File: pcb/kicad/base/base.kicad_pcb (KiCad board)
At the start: 2 copper layers, 381 parts, among them P1 J-Link SWD, P10 CONN_01X02, P11 CONN_01X02, P2 SMA, P3 CONN_01X02, P4 USB Micro B, P5 Button, P6 Button, P7 Button, P8 Button, P9 Button, Q1 IRLML2502, U1 SAMB11G18A-edit, U2 XBee-PRO_900HP, Y1 32.768kHz, Y2 26MHz

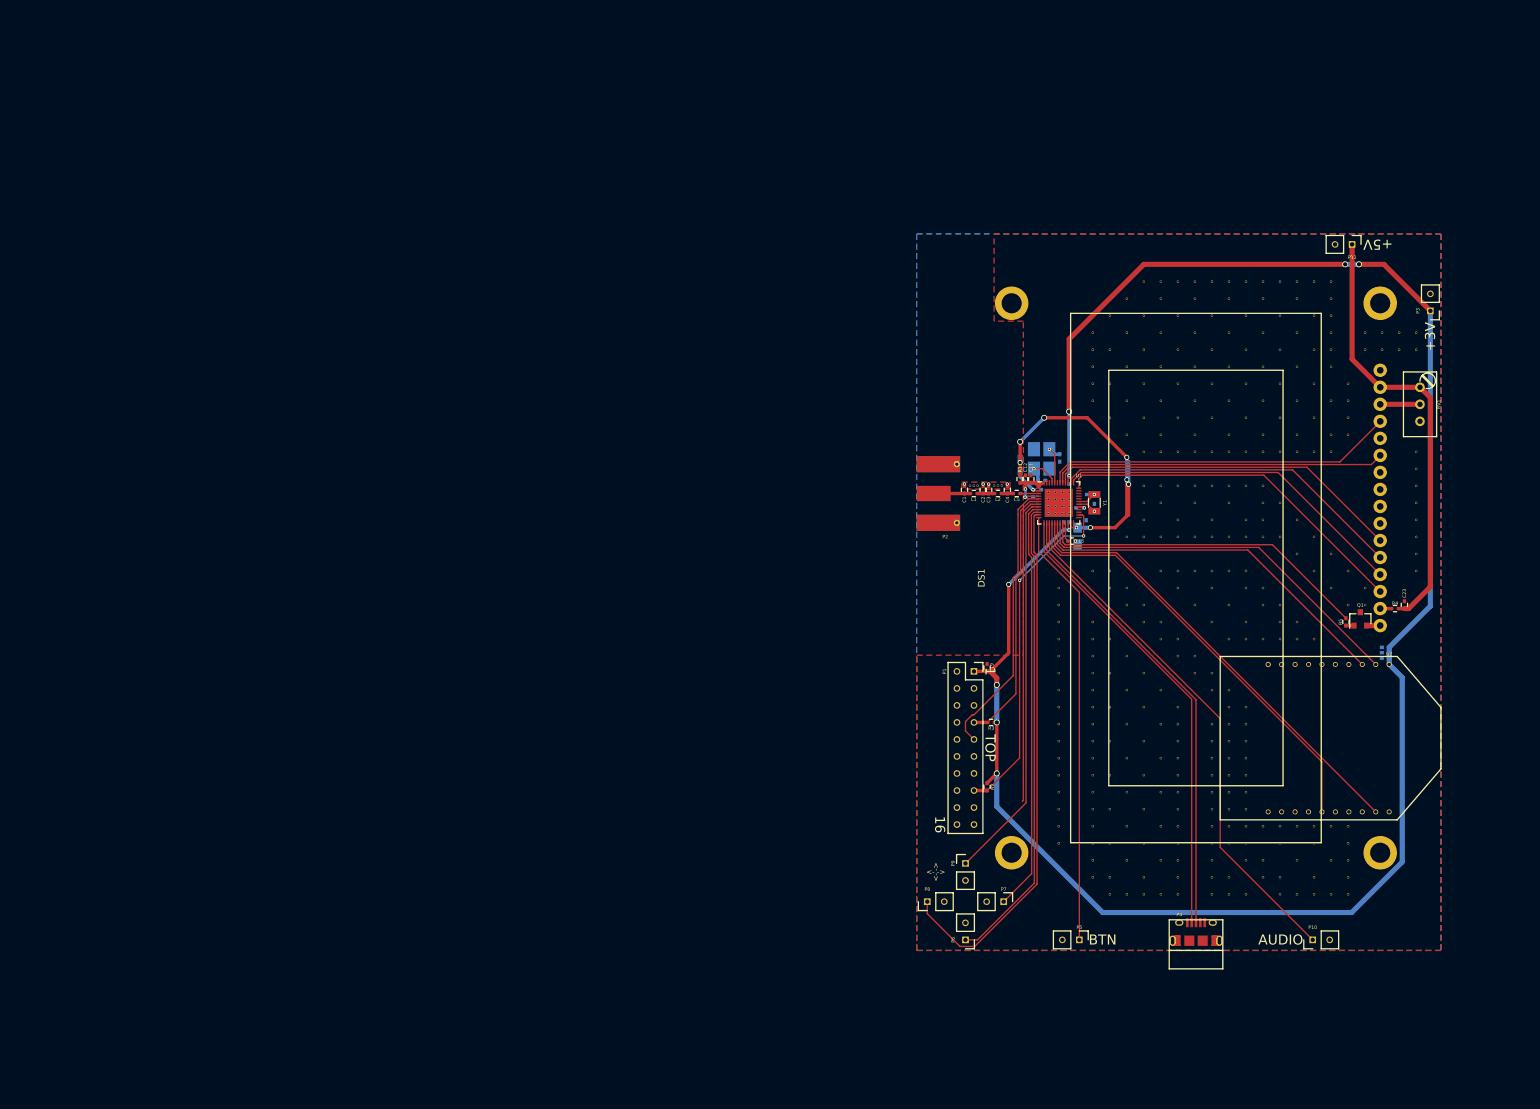
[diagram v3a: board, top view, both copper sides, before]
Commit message: Revamp base station layout
26MHz crystal moved to the top layer after reducing pad size. Slight
spacing with SMD components to avoid difficulties with hand soldering.
Component sections moved around for a more compact final layout. Antenna
section still needs to changed depending on transmission line matching
circuit. Traces to be finished.
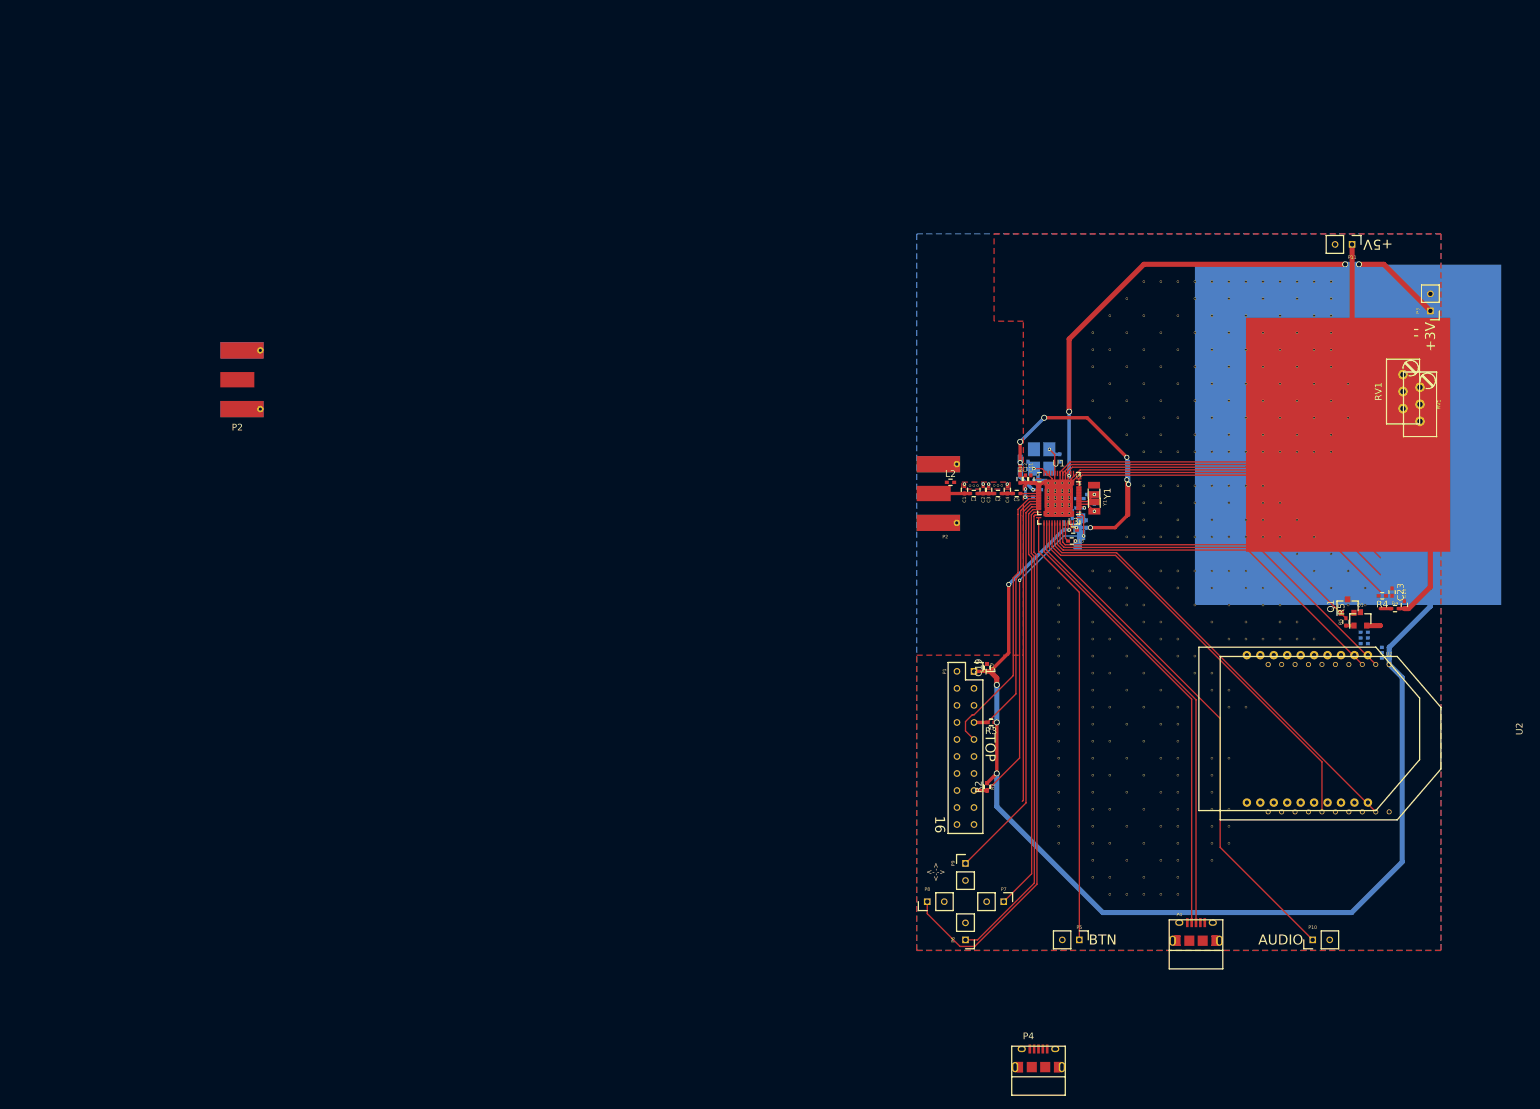
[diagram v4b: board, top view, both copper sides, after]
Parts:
- removed the C19 at (119.3, 95.3)
- removed DS1: LCD16X4, CFAH1604A
- removed the R2 at (119.3, 113.1)
- removed the R3 at (119.9, 103.5)
- removed the REF** at (178.3, 47.9)
- removed the REF** at (180.8, 47.9)
- removed the REF** at (183.4, 47.9)
- removed the REF** at (183.4, 65.7)
- removed the REF** at (183.4, 63.1)
- removed the REF** at (183.4, 73.3)
- removed the REF** at (183.4, 75.8)
- removed the REF** at (183.4, 70.7)
- removed the REF** at (183.4, 68.2)
- removed the REF** at (183.4, 78.4)
- removed the REF** at (173.2, 55.5)
- removed the REF** at (183.4, 80.9)
- removed the REF** at (173.2, 129.2)
- removed the REF** at (165.6, 129.2)
- removed the REF** at (163.0, 129.2)
- removed the REF** at (168.1, 129.2)
- removed the REF** at (170.7, 129.2)
- removed the REF** at (160.5, 124.1)
- removed the REF** at (160.5, 126.6)
- removed the REF** at (168.1, 126.6)
- removed the REF** at (163.0, 126.6)
- removed the REF** at (145.3, 40.3)
- removed the REF** at (165.6, 124.1)
- removed the REF** at (170.7, 124.1)
- removed the REF** at (173.2, 124.1)
- removed the REF** at (173.2, 126.6)
- removed the REF** at (173.2, 121.5)
- removed the REF** at (173.2, 119.0)
- removed the REF** at (165.6, 119.0)
- removed the REF** at (163.0, 119.0)
- removed the REF** at (168.1, 119.0)
- removed the REF** at (170.7, 119.0)
- removed the REF** at (135.1, 53.0)
- removed the REF** at (163.0, 121.5)
- removed the REF** at (168.1, 121.5)
- removed the REF** at (160.5, 119.0)
- removed the REF** at (158.0, 121.5)
- removed the REF** at (158.0, 119.0)
- removed the REF** at (158.0, 116.5)
- removed the REF** at (158.0, 124.1)
- removed the REF** at (158.0, 113.9)
- removed the REF** at (158.0, 111.4)
- removed the REF** at (158.0, 108.8)
- removed the REF** at (158.0, 103.8)
- removed the REF** at (158.0, 106.3)
- removed the REF** at (155.4, 129.2)
- removed the REF** at (152.9, 129.2)
- removed the REF** at (155.4, 126.6)
- removed the REF** at (152.9, 126.6)
- removed the REF** at (158.0, 129.2)
- removed the REF** at (152.9, 106.3)
- removed the REF** at (152.9, 103.8)
- removed the REF** at (155.4, 103.8)
- removed the REF** at (180.8, 45.3)
- removed the REF** at (155.4, 106.3)
- removed the REF** at (155.4, 113.9)
- removed the REF** at (155.4, 111.4)
- removed the REF** at (178.3, 45.3)
- removed the REF** at (175.7, 45.3)
- removed the REF** at (175.7, 47.9)
- added C12: 0.1uF, Capacitors_SMD:C_0402, B.Cu at (126.9, 66.5)
- added C13: 0.1uF, Capacitors_SMD:C_0402, B.Cu at (126.9, 67.4)
- added C14: 4.7uF 6.3V, Capacitors_SMD:C_0402, B.Cu at (132.0, 72.5)
- added C15: 0.1uF, Capacitors_SMD:C_0402, B.Cu at (131.6, 66.2)
- added C16: 2.2uF 6.3V, Capacitors_SMD:C_0402, B.Cu at (131.4, 73.9)
- added C18: 1.0uF, Capacitors_SMD:C_0402, B.Cu at (133.2, 70.1)
- added C19 (x2): C_Small, Capacitors_SMD:C_0402, F.Cu at (119.3, 95.3)
- added C20: 47pF, Capacitors_SMD:C_0402, B.Cu at (175.6, 91.7)
- added C21: 1.0uF, Capacitors_SMD:C_0402, B.Cu at (175.6, 90.9)
- added C22: 10uF, Capacitors_SMD:C_0402, B.Cu at (175.6, 90.0)
- added C23: 1.0uF, Capacitors_SMD:C_0402, F.Cu at (179.8, 84.1)
- added FB1: BLM03AG121SN1, Capacitors_SMD:C_0603_HandSoldering, B.Cu at (124.3, 65.5)
- added L2: 3nH, Capacitors_SMD:C_0402, F.Cu at (113.9, 67.7)
- added L3: 9.1nH, Capacitors_SMD:C_0402, F.Cu at (132.2, 74.8)
- added L4: 4.7uH, Capacitors_SMD:C_0805_HandSoldering, B.Cu at (133.4, 74.3)
- added P2: SMA, Misc:Molex_SMA_Jack_Edge_Mount, F.Cu at (9.16, 52.4)
- added P4: USB Micro B, Connectors:USB_Micro-B_10118194-000XLF, F.Cu at (127.0, 154.9)
- added Q1: IRLML2502, TO_SOT_Packages_SMD:SOT-23, F.Cu at (173.1, 86.1)
- added R1: 0, Capacitors_SMD:C_0402, B.Cu at (125.4, 65.1)
- added R2 (x2): 10k, Capacitors_SMD:C_0402, F.Cu at (119.3, 113.1)
- added R3 (x2): 100k, Capacitors_SMD:C_0402, F.Cu at (119.9, 103.5)
- added R4: 100, Capacitors_SMD:C_0402, F.Cu at (178.3, 84.6)
- added R5: 1k, Capacitors_SMD:C_0402, F.Cu at (170.9, 86.6)
- added RV1: 10k, Potentiometers:Potentiometer_Trimmer_Bourns_3296W, F.Cu at (181.4, 51.6)
- added U1: SAMB11G18A-edit, Housings:QFN-48-1EP_6x6mm_Pitch0.4mm, F.Cu at (130.0, 69.3)
- added U2: XBee-PRO_900HP, Digi_XBee-PRO_TH, F.Cu at (173.8, 104.5)
- added Y1: 32.768kHz, Crystals:Crystal_SMD_3215-2pin_3.2x1.5mm, F.Cu at (135.3, 69.3)
- REF**: value Via_Stitch_Dia0.356mm_Drill0.254mm -> Antenna_Shield
- REF**: value Via_Stitch_Dia0.356mm_Drill0.254mm -> (none)
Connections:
- REF** pad 1: GND -> (no net)
- REF** pad 1: GND -> /DISP_BRIGHT
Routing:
- net 78: track 0.00 -> 79.9 mm
- net /BTN_DOWN: track 79.9 -> 0.00 mm
- net 70: track 0.00 -> 78.5 mm
- net /AUDIO_SIG: track 78.5 -> 0.00 mm
- net 76: track 0.00 -> 70.2 mm
- net /BTN_RIGHT: track 70.2 -> 0.00 mm
- net 67: track 0.00 -> 68.9 mm
- net /Data+: track 68.9 -> 0.00 mm
- net 66: track 0.00 -> 68.8 mm
- net /Data-: track 68.8 -> 0.00 mm
- net 45: track 0.00 -> 67.7 mm
- net /UART_CTS: track 67.7 -> 0.00 mm
- net /+5V: track 65.5 -> 0.00 mm
- net 75: track 0.00 -> 65.5 mm
- net /BTN_HELP: track 65.5 -> 0.00 mm
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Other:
- net class Power removed

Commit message: Update base component placement and routing
New base station revision updated for a more complete prototype. Buttons
placed into layout, and SWD debugger pin header fixed.
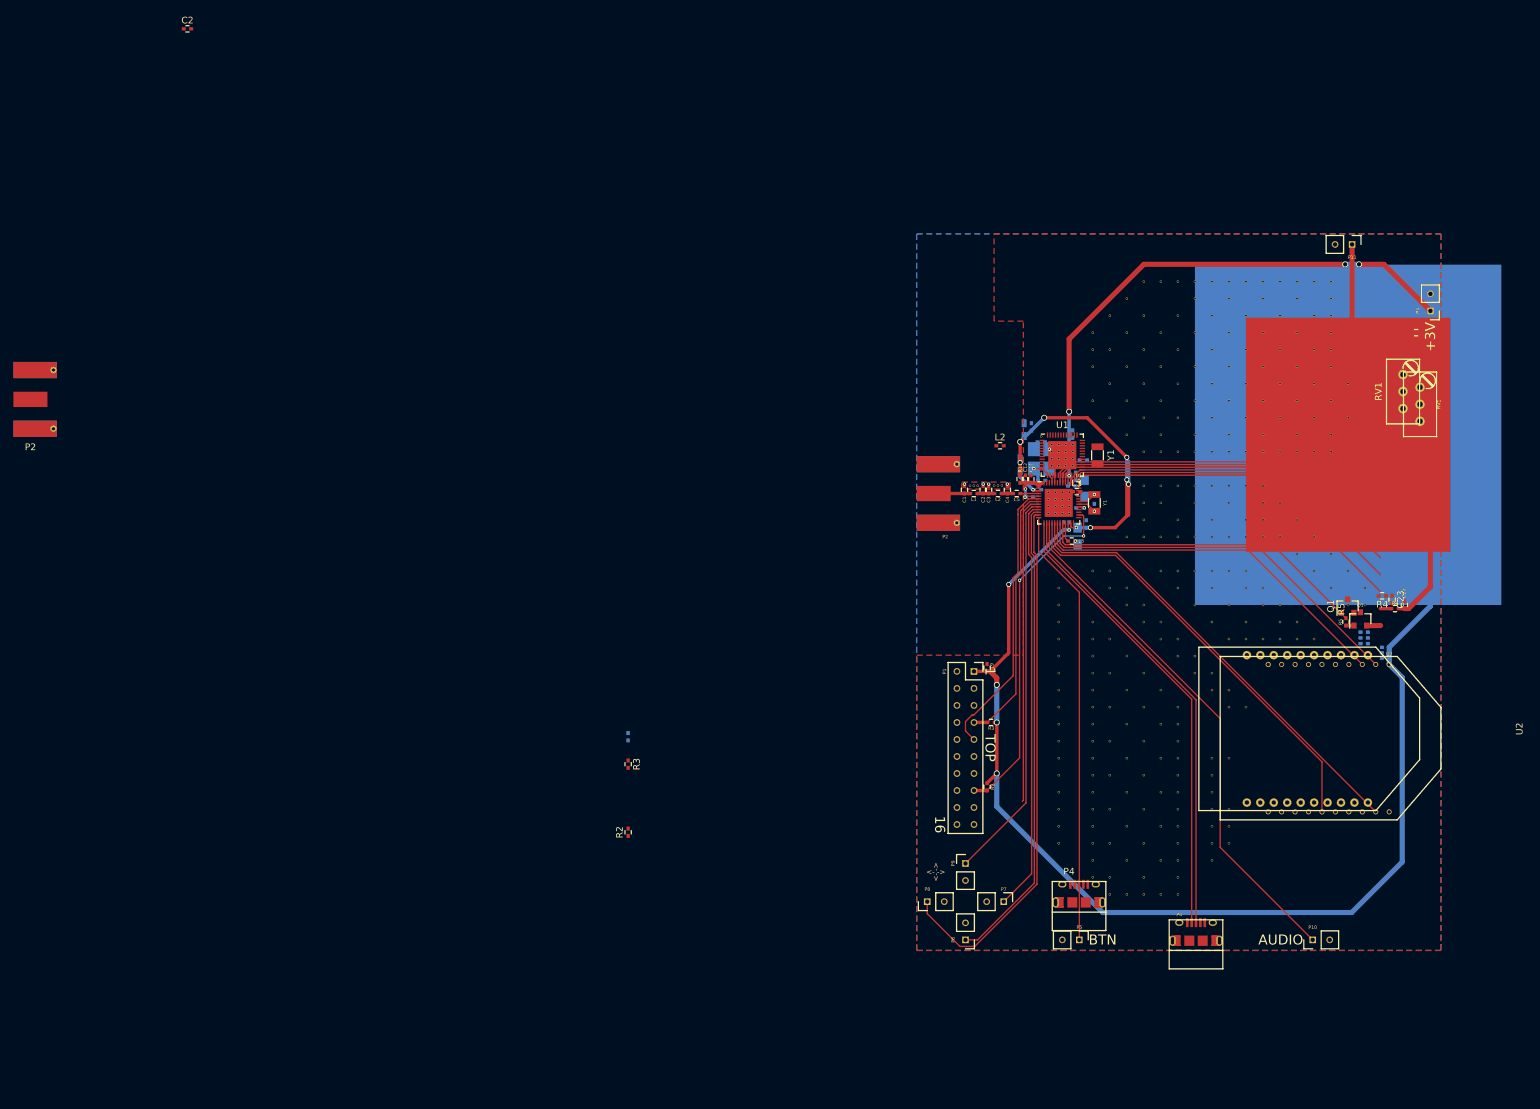
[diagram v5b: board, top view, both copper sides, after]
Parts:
- removed the C19 at (119.3, 95.3) (x2)
- removed the R2 at (119.3, 113.1) (x2)
- removed the R3 at (119.9, 103.5) (x2)
- added C19: C_Small, Capacitors_SMD:C_0402, B.Cu at (65.8, 105.6)
- added C19: C_Small, Capacitors_SMD:C_0402, F.Cu at (119.3, 95.3)
- added C2: DNI, Capacitors_SMD:C_0402, F.Cu at (0.00, 0.00)
- added R2: 10k, Capacitors_SMD:C_0402, F.Cu at (65.8, 119.9)
- added R2: 10k, Capacitors_SMD:C_0402, F.Cu at (119.3, 113.1)
- added R3: 100k, Capacitors_SMD:C_0402, F.Cu at (65.8, 109.7)
- added R3: 100k, Capacitors_SMD:C_0402, F.Cu at (119.9, 103.5)
- moved P2 31.0 mm to (-21.7, 55.3)
- moved P4 25.3 mm to (133.1, 130.4)
- moved L2 9.19 mm to (121.3, 62.2)
- moved C15 5.75 mm to (132.1, 60.5)
- moved C13 5.75 mm to (127.4, 61.7)
- moved FB1 5.75 mm to (124.8, 59.8)
- moved R1 5.75 mm to (125.9, 59.4)
- moved U1 5.75 mm to (130.6, 63.6)
- moved Y1 5.75 mm to (135.8, 63.6)
- moved C16 5.75 mm to (132.0, 68.2)
- moved L3 5.75 mm to (132.7, 69.1)
- moved L4 5.75 mm to (133.9, 68.6)
- moved C12 5.75 mm to (127.4, 60.8)
- moved C14 5.75 mm to (132.6, 66.8)
- moved C18 5.75 mm to (133.7, 64.4)
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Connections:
- U1 pad 10: /BTN_RIGHT -> /BTN_UP
- U1 pad 11: /BTN_DOWN -> /BTN_RIGHT
- U1 pad 9: /BTN_UP -> /BTN_DOWN
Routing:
- net 44: track 0.00 -> 64.6 mm
- net /DISP_RS: track 64.6 -> 0.00 mm
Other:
- board text added: "May 5, 2017"
- board text removed: "+5V"
- board text removed: "April 9, 2017"
